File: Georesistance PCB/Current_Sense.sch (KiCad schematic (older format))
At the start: 18 parts, among them Q5 LNC045R090, Q6 SI3430DV, Q8 SI3430DV, U4 RS8552

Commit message: Actually fixed the schematic
Hopefully for the last time
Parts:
- removed Q8: SI3430DV, Package_SO:TSOP-6_1.65x3.05mm_P0.95mm, symbol Device:Q_NMOS_DDGSDD
- added Q6: SI3430DV, Package_SO:TSOP-6_1.65x3.05mm_P0.95mm, symbol PMN30ENEAX:PMN30ENEAX
- Q5: renamed from Q6; symbol Device:Q_NMOS_DDGSDD -> PMN30ENEAX:PMN30ENEAX
- renumbered Q5 to Q7
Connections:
- wire segments 44 -> 57
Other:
- moved on the sheet: R13, R14
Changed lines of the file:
@@
 Wire Wire Line
 	1400 1900 1400 1800
-Text GLabel 2800 1200 0    50   Input ~ 0
+Text GLabel 1900 2650 0    50   Input ~ 0
 Pasak_B
-Wire Wire Line
-	2800 1200 2800 1350
-Text GLabel 2500 1550 0    50   Input ~ 0
+Text GLabel 1150 3350 0    50   Input ~ 0
 LVL_B_5V
 $Comp
 L Device:R_US R13
 U 1 1 613E7D7A
-P 2800 2050
-F 0 "R13" H 2868 2096 50  0000 L CNN
-F 1 "400m" H 2868 2005 50  0000 L CNN
-F 2 "Resistor_SMD:R_2512_6332Metric_Pad1.40x3.35mm_HandSolder" V 2840 2040 50  0001 C CNN
-F 3 "~" H 2800 2050 50  0001 C CNN
-	1    2800 2050
+P 2750 4200
+F 0 "R13" H 2818 4246 50  0000 L CNN
+F 1 "400m" H 2818 4155 50  0000 L CNN
+F 2 "Resistor_SMD:R_2512_6332Metric_Pad1.40x3.35mm_HandSolder" V 2790 4190 50  0001 C CNN
+F 3 "~" H 2750 4200 50  0001 C CNN
+	1    2750 4200
 	1    0    0    -1
 $EndComp
@@
 L power:GND #PWR019
 U 1 1 613E7D80
-P 2800 2200
-F 0 "#PWR019" H 2800 1950 50  0001 C CNN
-F 1 "GND" H 2805 2027 50  0000 C CNN
-F 2 "" H 2800 2200 50  0001 C CNN
-F 3 "" H 2800 2200 50  0001 C CNN
-	1    2800 2200
-	1    0    0    -1
-$EndComp
-Wire Wire Line
-	2800 1800 2600 1800
-Wire Wire Line
-	2800 1900 2800 1800
+P 2750 4350
+F 0 "#PWR019" H 2750 4100 50  0001 C CNN
+F 1 "GND" H 2755 4177 50  0000 C CNN
+F 2 "" H 2750 4350 50  0001 C CNN
+F 3 "" H 2750 4350 50  0001 C CNN
+	1    2750 4350
+	1    0    0    -1
+$EndComp
+Wire Wire Line
+	2750 3950 2550 3950
+Wire Wire Line
+	2750 4050 2750 3950
 $Comp
 L Device:Opamp_Dual_Generic U4
@@
 Wire Wire Line
 	8750 4350 8300 4350
-Text Label 4750 1850 0    50   ~ 0
+Text Label 2550 6100 0    50   ~ 0
 R_C
 Wire Wire Line
-	4950 1950 4950 1850
-Wire Wire Line
-	4950 1750 4950 1850
-Connection ~ 4950 1850
-Wire Wire Line
-	4950 1850 4750 1850
+	2750 6200 2750 6100
+Connection ~ 2750 6100
+Wire Wire Line
+	2750 6100 2550 6100
 $Comp
 L power:GND #PWR020
 U 1 1 613E9B1D
-P 4950 2250
-F 0 "#PWR020" H 4950 2000 50  0001 C CNN
-F 1 "GND" H 4955 2077 50  0000 C CNN
-F 2 "" H 4950 2250 50  0001 C CNN
-F 3 "" H 4950 2250 50  0001 C CNN
-	1    4950 2250
+P 2750 6500
+F 0 "#PWR020" H 2750 6250 50  0001 C CNN
+F 1 "GND" H 2755 6327 50  0000 C CNN
+F 2 "" H 2750 6500 50  0001 C CNN
+F 3 "" H 2750 6500 50  0001 C CNN
+	1    2750 6500
 	1    0    0    -1
 $EndComp
@@
 L Device:R_US R14
 U 1 1 613E9B17
-P 4950 2100
-F 0 "R14" H 5018 2146 50  0000 L CNN
-F 1 "6.2" H 5018 2055 50  0000 L CNN
-F 2 "Resistor_SMD:R_0805_2012Metric_Pad1.20x1.40mm_HandSolder" V 4990 2090 50  0001 C CNN
-F 3 "~" H 4950 2100 50  0001 C CNN
-	1    4950 2100
-	1    0    0    -1
-$EndComp
-Text GLabel 4950 1200 0    50   Input ~ 0
-Pasak_B
-Wire Wire Line
-	4950 1200 4950 1350
-Text GLabel 4650 1550 0    50   Input ~ 0
-LVL_C_5V
+P 2750 6350
+F 0 "R14" H 2818 6396 50  0000 L CNN
+F 1 "6.2" H 2818 6305 50  0000 L CNN
+F 2 "Resistor_SMD:R_0805_2012Metric_Pad1.20x1.40mm_HandSolder" V 2790 6340 50  0001 C CNN
+F 3 "~" H 2750 6350 50  0001 C CNN
+	1    2750 6350
+	1    0    0    -1
+$EndComp
 $Comp
 L Device:R_POT_TRIM_US RV2
@@
 	7200 4350 7650 4350
 $Comp
-L Device:Q_NMOS_DGS Q5
+L Device:Q_NMOS_DGS Q7
 U 1 1 616CCFBF
 P 1300 1500
-F 0 "Q5" H 1505 1546 50  0000 L CNN
+F 0 "Q7" H 1505 1546 50  0000 L CNN
 F 1 "LNC045R090" H 1505 1455 50  0000 L CNN
 F 2 "Package_TO_SOT_THT:TO-220-3_Vertical" H 1500 1600 50  0001 C CNN
@@
 Connection ~ 1400 1800
 $Comp
-L Device:Q_NMOS_DDGSDD Q6
+L PMN30ENEAX:PMN30ENEAX Q5
 U 1 1 616D459D
-P 2700 1550
-F 0 "Q6" H 2905 1626 50  0000 L CNN
-F 1 "SI3430DV" H 2905 1535 50  0000 L CNN
-F 2 "Package_SO:TSOP-6_1.65x3.05mm_P0.95mm" H 2900 1650 50  0001 C CNN
-F 3 "~" H 2700 1550 50  0001 C CNN
-	1    2700 1550
-	1    0    0    -1
-$EndComp
-$Comp
-L Device:Q_NMOS_DDGSDD Q8
-U 1 1 616D58F2
-P 4850 1550
-F 0 "Q8" H 5055 1626 50  0000 L CNN
-F 1 "SI3430DV" H 5055 1535 50  0000 L CNN
-F 2 "Package_SO:TSOP-6_1.65x3.05mm_P0.95mm" H 5050 1650 50  0001 C CNN
-F 3 "~" H 4850 1550 50  0001 C CNN
-	1    4850 1550
-	1    0    0    -1
-$EndComp
-Wire Wire Line
-	2800 1750 2800 1800
-Connection ~ 2800 1800
+P 1150 3150
+F 0 "Q5" H 1355 3226 50  0000 L CNN
+F 1 "SI3430DV" H 1355 3135 50  0000 L CNN
+F 2 "Package_SO:TSOP-6_1.65x3.05mm_P0.95mm" H 1350 3250 50  0001 C CNN
+F 3 "~" H 1150 3150 50  0001 C CNN
+	1    1150 3150
+	1    0    0    -1
+$EndComp
+Connection ~ 2750 3950
+Wire Wire Line
+	1900 2650 1900 2800
+Text Label 2600 3950 0    50   ~ 0
+R_B
+Wire Wire Line
+	2750 3350 2750 3950
+Wire Wire Line
+	1900 2800 2750 2800
+Wire Wire Line
+	2750 2800 2750 3150
+Wire Wire Line
+	2750 3250 2750 3150
+Connection ~ 2750 3150
+Wire Wire Line
+	1150 3250 1150 3150
+Wire Wire Line
+	1150 3150 1150 2800
+Wire Wire Line
+	1150 2800 1900 2800
+Connection ~ 1150 3150
+Connection ~ 1900 2800
+Text GLabel 1900 4750 0    50   Input ~ 0
+Pasak_B
+$Comp
+L PMN30ENEAX:PMN30ENEAX Q6
+U 1 1 61700F15
+P 1150 5250
+F 0 "Q6" H 1355 5326 50  0000 L CNN
+F 1 "SI3430DV" H 1355 5235 50  0000 L CNN
+F 2 "Package_SO:TSOP-6_1.65x3.05mm_P0.95mm" H 1350 5350 50  0001 C CNN
+F 3 "~" H 1150 5250 50  0001 C CNN
+	1    1150 5250
+	1    0    0    -1
+$EndComp
+Wire Wire Line
+	1900 4750 1900 4900
+Wire Wire Line
+	1900 4900 2750 4900
+Wire Wire Line
+	2750 4900 2750 5250
+Wire Wire Line
+	2750 5350 2750 5250
+Connection ~ 2750 5250
+Wire Wire Line
+	1150 5350 1150 5250
+Wire Wire Line
+	1150 5250 1150 4900
+Wire Wire Line
+	1150 4900 1900 4900
+Connection ~ 1150 5250
+Connection ~ 1900 4900
+Text GLabel 1150 5450 0    50   Input ~ 0
+LVL_C_5V
+Wire Wire Line
+	2750 5400 2750 5450
+Connection ~ 2750 5450
+Wire Wire Line
+	2750 5450 2750 6100
 $EndSCHEMATC

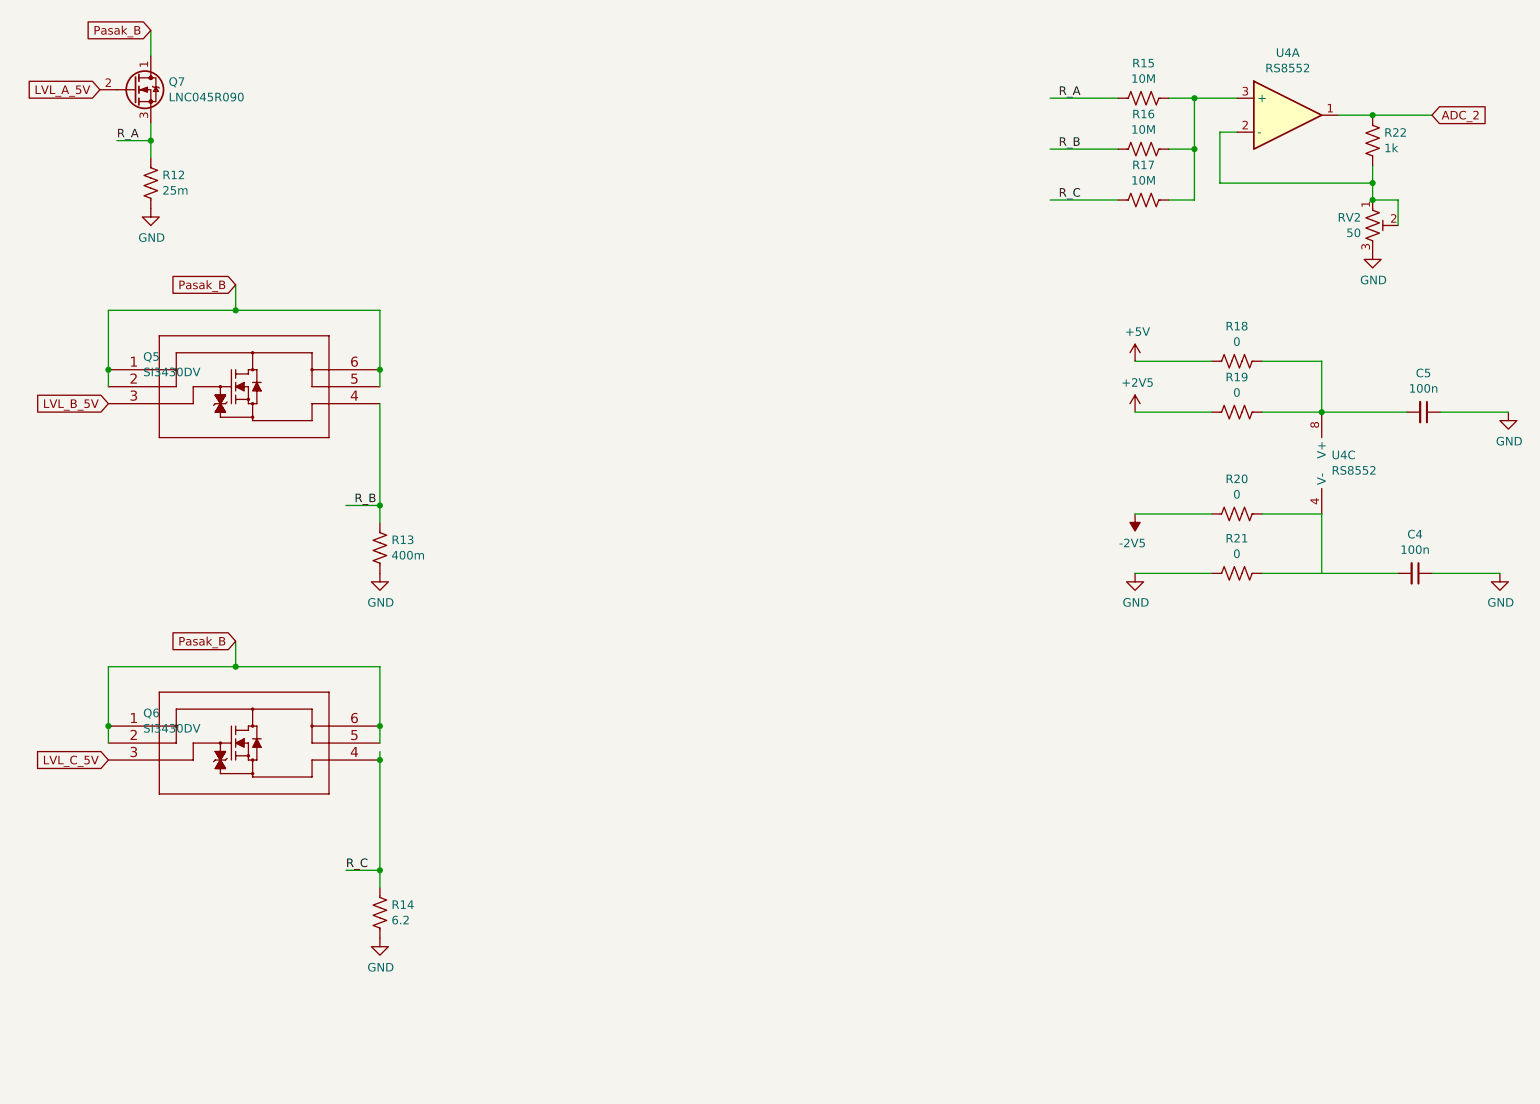
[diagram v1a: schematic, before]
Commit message: Added the PCB layout and simplified schematic
deleted jumper, and fixed misconnection
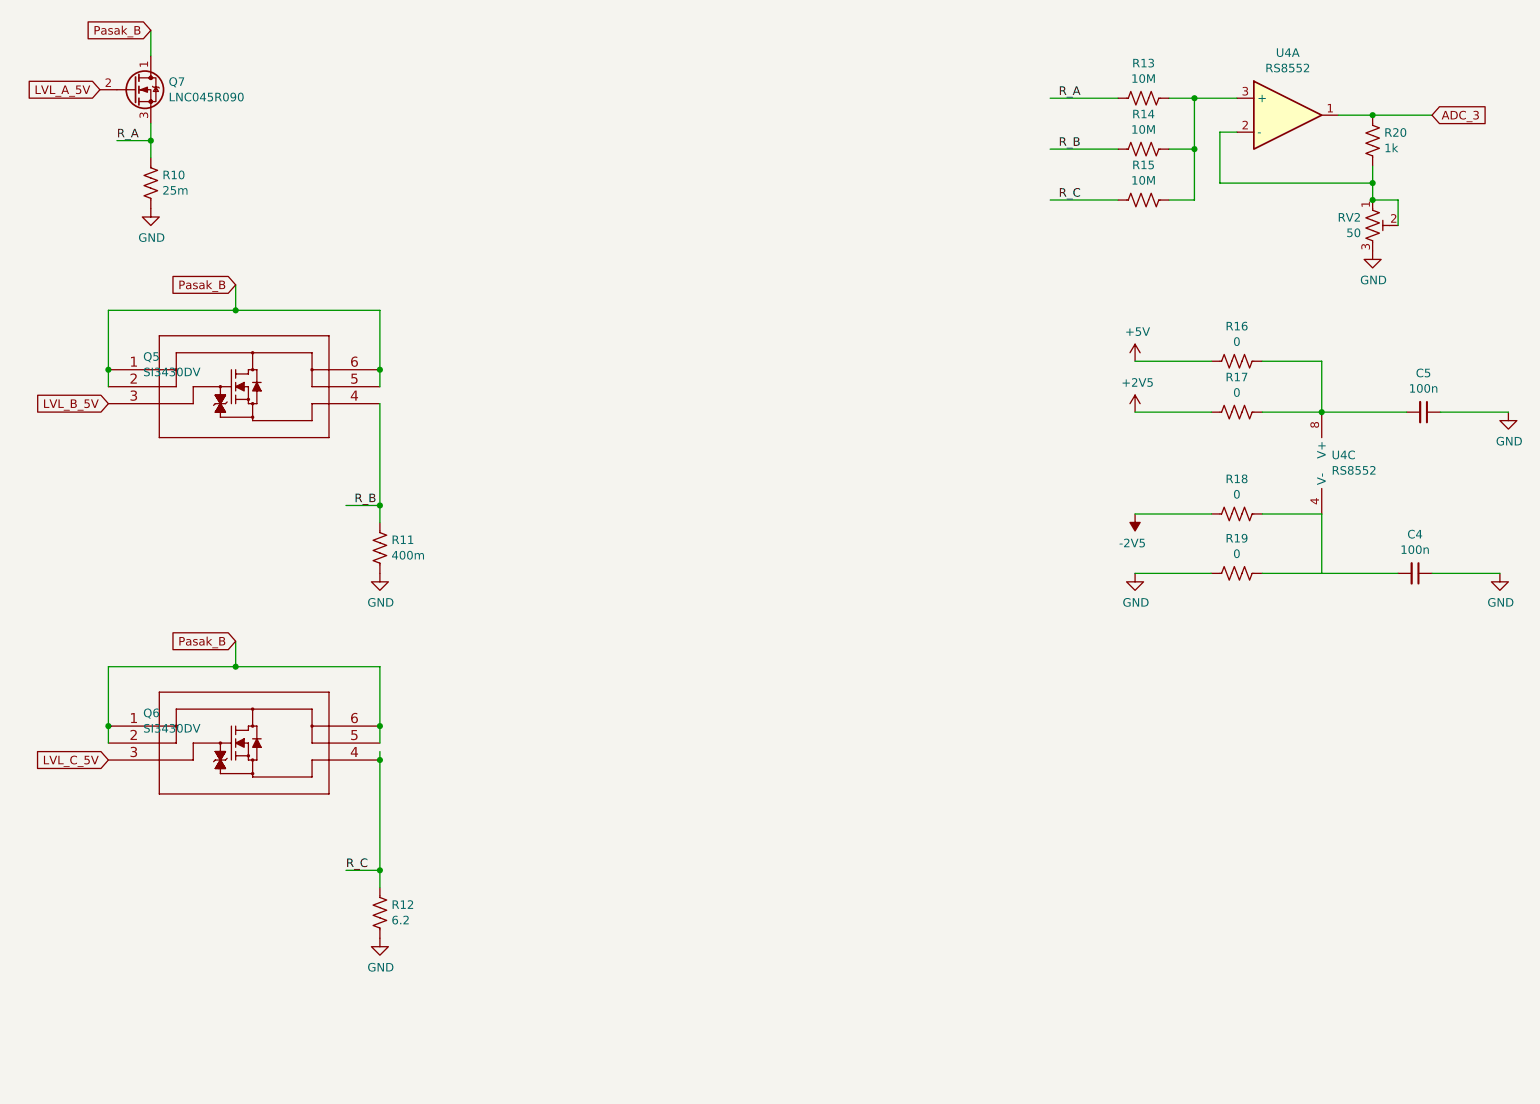
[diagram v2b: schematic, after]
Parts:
- renumbered R12 to R10, R13 to R11, R14 to R12, R15 to R13, R16 to R14, R17 to R15, R18 to R16, R19 to R17, R20 to R18, R21 to R19, R22 to R20
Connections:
- net labels added: ADC_3
- net labels removed: ADC_2
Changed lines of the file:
@@
 Wire Wire Line
 	1400 1150 1400 1300
-Text GLabel 1100 1500 0    50   Input ~ 0
-LVL_A_5V
-$Comp
-L Device:R_US R12
+$Comp
+L Device:R_US R10
 U 1 1 613E28F9
 P 1400 2050
-F 0 "R12" H 1468 2096 50  0000 L CNN
+F 0 "R10" H 1468 2096 50  0000 L CNN
 F 1 "25m" H 1468 2005 50  0000 L CNN
 F 2 "Resistor_SMD:R_0603_1608Metric_Pad0.98x0.95mm_HandSolder" V 1440 2040 50  0001 C CNN
@@
 $EndComp
 $Comp
-L power:GND #PWR018
+L power:GND #PWR017
 U 1 1 613E36B2
 P 1400 2200
-F 0 "#PWR018" H 1400 1950 50  0001 C CNN
+F 0 "#PWR017" H 1400 1950 50  0001 C CNN
 F 1 "GND" H 1405 2027 50  0000 C CNN
 F 2 "" H 1400 2200 50  0001 C CNN
@@
 LVL_B_5V
 $Comp
-L Device:R_US R13
+L Device:R_US R11
 U 1 1 613E7D7A
 P 2750 4200
-F 0 "R13" H 2818 4246 50  0000 L CNN
+F 0 "R11" H 2818 4246 50  0000 L CNN
 F 1 "400m" H 2818 4155 50  0000 L CNN
 F 2 "Resistor_SMD:R_2512_6332Metric_Pad1.40x3.35mm_HandSolder" V 2790 4190 50  0001 C CNN
@@
 $EndComp
 $Comp
-L power:GND #PWR019
+L power:GND #PWR018
 U 1 1 613E7D80
 P 2750 4350
-F 0 "#PWR019" H 2750 4100 50  0001 C CNN
+F 0 "#PWR018" H 2750 4100 50  0001 C CNN
 F 1 "GND" H 2755 4177 50  0000 C CNN
 F 2 "" H 2750 4350 50  0001 C CNN
@@
 $EndComp
 $Comp
-L Device:R_US R15
+L Device:R_US R13
 U 1 1 613F6EC7
 P 7250 1550
-F 0 "R15" V 7045 1550 50  0000 C CNN
+F 0 "R13" V 7045 1550 50  0000 C CNN
 F 1 "10M" V 7136 1550 50  0000 C CNN
 F 2 "Resistor_THT:R_Axial_DIN0207_L6.3mm_D2.5mm_P7.62mm_Horizontal" V 7290 1540 50  0001 C CNN
@@
 	7100 1550 6700 1550
 $Comp
-L Device:R_US R16
+L Device:R_US R14
 U 1 1 613F7F66
 P 7250 1850
-F 0 "R16" V 7045 1850 50  0000 C CNN
+F 0 "R14" V 7045 1850 50  0000 C CNN
 F 1 "10M" V 7136 1850 50  0000 C CNN
 F 2 "Resistor_THT:R_Axial_DIN0207_L6.3mm_D2.5mm_P7.62mm_Horizontal" V 7290 1840 50  0001 C CNN
@@
 $EndComp
 $Comp
-L Device:R_US R17
+L Device:R_US R15
 U 1 1 613F8BC5
 P 7250 2150
-F 0 "R17" V 7045 2150 50  0000 C CNN
+F 0 "R15" V 7045 2150 50  0000 C CNN
 F 1 "10M" V 7136 2150 50  0000 C CNN
 F 2 "Resistor_THT:R_Axial_DIN0207_L6.3mm_D2.5mm_P7.62mm_Horizontal" V 7290 2140 50  0001 C CNN
@@
 R_C
 $Comp
-L Device:R_US R22
+L Device:R_US R20
 U 1 1 613FF83E
 P 8600 1800
-F 0 "R22" H 8668 1846 50  0000 L CNN
+F 0 "R20" H 8668 1846 50  0000 L CNN
 F 1 "1k" H 8668 1755 50  0000 L CNN
 F 2 "Resistor_THT:R_Axial_DIN0207_L6.3mm_D2.5mm_P7.62mm_Horizontal" V 8640 1790 50  0001 C CNN
@@
 Connection ~ 8600 2050
 $Comp
-L power:GND #PWR025
+L power:GND #PWR024
 U 1 1 61403313
 P 8600 2450
-F 0 "#PWR025" H 8600 2200 50  0001 C CNN
+F 0 "#PWR024" H 8600 2200 50  0001 C CNN
 F 1 "GND" H 8605 2277 50  0000 C CNN
 F 2 "" H 8600 2450 50  0001 C CNN
@@
 Connection ~ 8600 1650
 Text GLabel 8950 1650 2    50   Input ~ 0
-ADC_2
-$Comp
-L power:+5V #PWR021
+ADC_3
+$Comp
+L power:+5V #PWR020
 U 1 1 613F5609
 P 7200 3100
-F 0 "#PWR021" H 7200 2950 50  0001 C CNN
+F 0 "#PWR020" H 7200 2950 50  0001 C CNN
 F 1 "+5V" H 7215 3273 50  0000 C CNN
 F 2 "" H 7200 3100 50  0001 C CNN
@@
 $EndComp
 $Comp
-L power:GND #PWR024
+L power:GND #PWR023
 U 1 1 613F70B2
 P 7200 4350
-F 0 "#PWR024" H 7200 4100 50  0001 C CNN
+F 0 "#PWR023" H 7200 4100 50  0001 C CNN
 F 1 "GND" H 7205 4177 50  0000 C CNN
 F 2 "" H 7200 4350 50  0001 C CNN
@@
 $EndComp
 $Comp
-L power:GND #PWR026
+L power:GND #PWR025
 U 1 1 61464306
 P 9350 4350
-F 0 "#PWR026" H 9350 4100 50  0001 C CNN
+F 0 "#PWR025" H 9350 4100 50  0001 C CNN
 F 1 "GND" H 9355 4177 50  0000 C CNN
 F 2 "" H 9350 4350 50  0001 C CNN
@@
 $EndComp
 $Comp
-L power:GND #PWR027
+L power:GND #PWR026
 U 1 1 61464779
 P 9400 3400
-F 0 "#PWR027" H 9400 3150 50  0001 C CNN
+F 0 "#PWR026" H 9400 3150 50  0001 C CNN
 F 1 "GND" H 9405 3227 50  0000 C CNN
 F 2 "" H 9400 3400 50  0001 C CNN
@@
 	2750 6100 2550 6100
 $Comp
-L power:GND #PWR020
+L power:GND #PWR019
 U 1 1 613E9B1D
 P 2750 6500
-F 0 "#PWR020" H 2750 6250 50  0001 C CNN
+F 0 "#PWR019" H 2750 6250 50  0001 C CNN
 F 1 "GND" H 2755 6327 50  0000 C CNN
 F 2 "" H 2750 6500 50  0001 C CNN
@@
 $EndComp
 $Comp
-L Device:R_US R14
+L Device:R_US R12
 U 1 1 613E9B17
 P 2750 6350
-F 0 "R14" H 2818 6396 50  0000 L CNN
+F 0 "R12" H 2818 6396 50  0000 L CNN
 F 1 "6.2" H 2818 6305 50  0000 L CNN
 F 2 "Resistor_SMD:R_0805_2012Metric_Pad1.20x1.40mm_HandSolder" V 2790 6340 50  0001 C CNN
@@
 	8300 4000 8300 4350
 $Comp
-L power:-2V5 #PWR023
+L power:-2V5 #PWR022
 U 1 1 61406039
 P 7200 4000
-F 0 "#PWR023" H 7200 4100 50  0001 C CNN
+F 0 "#PWR022" H 7200 4100 50  0001 C CNN
 F 1 "-2V5" H 7215 4173 50  0000 C CNN
 F 2 "" H 7200 4000 50  0001 C CNN
@@
 $EndComp
 $Comp
-L power:+2V5 #PWR022
+L power:+2V5 #PWR021
 U 1 1 61404F3B
 P 7200 3400
-F 0 "#PWR022" H 7200 3250 50  0001 C CNN
+F 0 "#PWR021" H 7200 3250 50  0001 C CNN
 F 1 "+2V5" H 7215 3573 50  0000 C CNN
 F 2 "" H 7200 3400 50  0001 C CNN
@@
 P 7800 3100
 AR Path="/613F3D44/615BF29A" Ref="R?"  Part="1"
-AR Path="/613FF101/615BF29A" Ref="R18"  Part="1"
-F 0 "R18" V 7595 3100 50  0000 C CNN
+AR Path="/613FF101/615BF29A" Ref="R16"  Part="1"
+F 0 "R16" V 7595 3100 50  0000 C CNN
 F 1 "0" V 7686 3100 50  0000 C CNN
 F 2 "Resistor_SMD:R_0402_1005Metric_Pad0.72x0.64mm_HandSolder" V 7840 3090 50  0001 C CNN
@@
 P 7800 3400
 AR Path="/613F3D44/615CD95B" Ref="R?"  Part="1"
-AR Path="/613FF101/615CD95B" Ref="R19"  Part="1"
-F 0 "R19" V 7595 3400 50  0000 C CNN
+AR Path="/613FF101/615CD95B" Ref="R17"  Part="1"
+F 0 "R17" V 7595 3400 50  0000 C CNN
 F 1 "0" V 7686 3400 50  0000 C CNN
 F 2 "Resistor_SMD:R_0402_1005Metric_Pad0.72x0.64mm_HandSolder" V 7840 3390 50  0001 C CNN
@@
 P 7800 4000
 AR Path="/613F3D44/615D34B1" Ref="R?"  Part="1"
-AR Path="/613FF101/615D34B1" Ref="R20"  Part="1"
-F 0 "R20" V 7595 4000 50  0000 C CNN
+AR Path="/613FF101/615D34B1" Ref="R18"  Part="1"
+F 0 "R18" V 7595 4000 50  0000 C CNN
 F 1 "0" V 7686 4000 50  0000 C CNN
 F 2 "Resistor_SMD:R_0402_1005Metric_Pad0.72x0.64mm_HandSolder" V 7840 3990 50  0001 C CNN
@@
 P 7800 4350
 AR Path="/613F3D44/615D4076" Ref="R?"  Part="1"
-AR Path="/613FF101/615D4076" Ref="R21"  Part="1"
-F 0 "R21" V 7595 4350 50  0000 C CNN
+AR Path="/613FF101/615D4076" Ref="R19"  Part="1"
+F 0 "R19" V 7595 4350 50  0000 C CNN
 F 1 "0" V 7686 4350 50  0000 C CNN
 F 2 "Resistor_SMD:R_0402_1005Metric_Pad0.72x0.64mm_HandSolder" V 7840 4340 50  0001 C CNN
@@
 Connection ~ 1150 5250
 Connection ~ 1900 4900
+Wire Wire Line
+	2750 5400 2750 5450
+Connection ~ 2750 5450
+Wire Wire Line
+	2750 5450 2750 6100
 Text GLabel 1150 5450 0    50   Input ~ 0
 LVL_C_5V
-Wire Wire Line
-	2750 5400 2750 5450
-Connection ~ 2750 5450
-Wire Wire Line
-	2750 5450 2750 6100
+Text GLabel 1100 1500 0    50   Input ~ 0
+LVL_A_5V
 $EndSCHEMATC

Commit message: added things
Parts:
- added C? (x2): 2.2u, Capacitor_SMD:C_0402_1005Metric_Pad0.74x0.62mm_HandSolder, symbol Device:C_Small
- added C?: 1u, Capacitor_SMD:C_0402_1005Metric_Pad0.74x0.62mm_HandSolder, symbol Device:C_Small
- added R? (x2): 180, Resistor_THT:R_Axial_DIN0207_L6.3mm_D2.5mm_P7.62mm_Horizontal, symbol Device:R_US
- added U?: LM2776, Package_TO_SOT_SMD:SOT-23-6, symbol Regulator_SwitchedCapacitor:LM2776
- added U?: LM337L_TO92, Package_TO_SOT_THT:TO-92_Inline, symbol Regulator_Linear:LM337L_TO92
- added U?: XC6206P252MR, Package_TO_SOT_SMD:SOT-23, symbol Regulator_Linear:AP2127N-2.5
- Q7: value LNC045R090 -> LNC10R180
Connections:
- net labels added: -5V
- wire segments 57 -> 74
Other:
- moved on the sheet: C4, C5, R13, R14, R15, R16, R17, R18, R19, R20, RV2, U4A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
